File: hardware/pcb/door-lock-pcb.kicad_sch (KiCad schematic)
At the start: 53 parts, among them J1 105162-0001, J2 Conn_01x08, J4 Conn_01x04, J6 Conn_01x02, J7 Conn_01x02, Q1 SI2308DS, Q3 DMN6068LK3, U1 ESP32-DEVKIT-V1, U2 DS1307Z+, U3 MP1470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

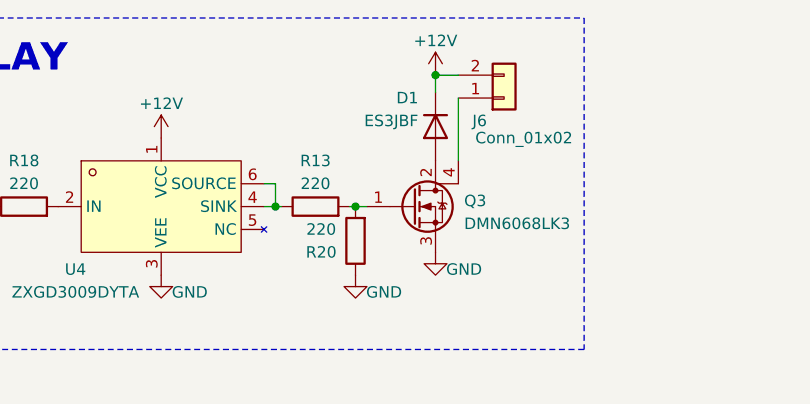
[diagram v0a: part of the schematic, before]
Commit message: fixed error with mosfet drain
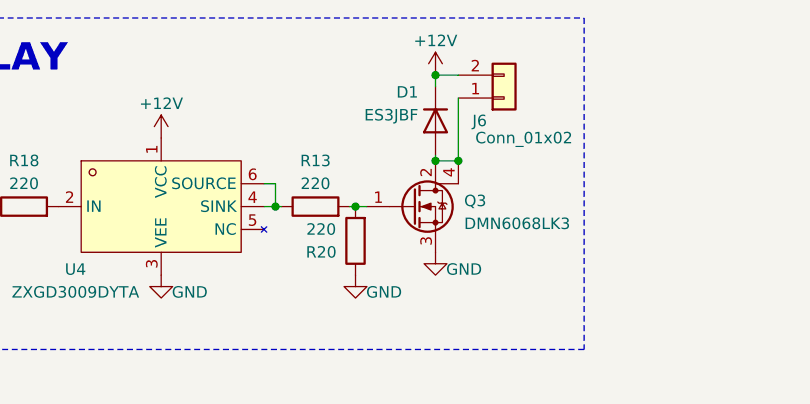
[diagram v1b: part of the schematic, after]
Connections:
- net at J6.1 (Pin_1), Q3.4 (D): now also D1.2 (A), Q3.2 (D)
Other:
- moved on the sheet: D1
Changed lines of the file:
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@@
   (junction (at 50.165 124.46) (diameter 0) (color 0 0 0 0)
   )
+  (junction (at 179.705 32.385) (diameter 0) (color 0 0 0 0)
+  )
   (junction (at 52.07 189.23) (diameter 0) (color 0 0 0 0)
   )
   (junction (at 186.055 134.62) (diameter 0) (color 0 0 0 0)
+  )
+  (junction (at 177.165 32.385) (diameter 0) (color 0 0 0 0)
   )
   (junction (at 215.265 137.16) (diameter 0) (color 0 0 0 0)
@@
     (stroke (width 0) (type default))
   )
+  (wire (pts (xy 177.165 31.75) (xy 177.165 32.385))
+    (stroke (width 0) (type default))
+  )
   (wire (pts (xy 186.055 144.78) (xy 186.055 139.7))
     (stroke (width 0) (type default))
@@
     (stroke (width 0) (type default))
   )
+  (wire (pts (xy 177.165 32.385) (xy 179.705 32.385))
+    (stroke (width 0) (type default))
+  )
   (wire (pts (xy 168.275 37.465) (xy 169.545 37.465))
     (stroke (width 0) (type default))
@@
     (stroke (width 0) (type default))
   )
-  (wire (pts (xy 177.165 22.86) (xy 177.165 24.765))
+  (wire (pts (xy 177.165 22.86) (xy 177.165 24.13))
     (stroke (width 0) (type default))
   )
@@
     )
   )
-  (symbol (lib_id "Device:D") (at 177.165 28.575 90) (mirror x) (unit 1)
-    (in_bom yes) (on_board yes) (dnp no)
-    (property "Reference" "D1" (at 175.26 25.4 90)
-      (effects (font (size 1.27 1.27)) (justify left))
-    )
-    (property "Value" "ES3JBF" (at 175.26 27.94 90)
-      (effects (font (size 1.27 1.27)) (justify left))
-    )
-    (property "Footprint" "Diode_SMD:D_SMC" (at 177.165 28.575 0)
-      (effects (font (size 1.27 1.27)) hide)
-    )
-    (property "Datasheet" "~" (at 177.165 28.575 0)
-      (effects (font (size 1.27 1.27)) hide)
-    )
-    (property "Sim.Device" "D" (at 177.165 28.575 0)
-      (effects (font (size 1.27 1.27)) hide)
-    )
-    (property "Sim.Pins" "1=K 2=A" (at 177.165 28.575 0)
-      (effects (font (size 1.27 1.27)) hide)
-    )
-    (property "LCSC" "C3011135" (at 177.165 28.575 90)
-      (effects (font (size 1.27 1.27)) hide)
-    )
+  (symbol (lib_id "Device:D") (at 177.165 27.94 90) (mirror x) (unit 1)
+    (in_bom yes) (on_board yes) (dnp no)
+    (property "Reference" "D1" (at 175.26 24.765 90)
+      (effects (font (size 1.27 1.27)) (justify left))
+    )
+    (property "Value" "ES3JBF" (at 175.26 27.305 90)
+      (effects (font (size 1.27 1.27)) (justify left))
+    )
+    (property "Footprint" "Diode_SMD:D_SMC" (at 177.165 27.94 0)
+      (effects (font (size 1.27 1.27)) hide)
+    )
+    (property "Datasheet" "~" (at 177.165 27.94 0)
+      (effects (font (size 1.27 1.27)) hide)
+    )
+    (property "Sim.Device" "D" (at 177.165 27.94 0)
+      (effects (font (size 1.27 1.27)) hide)
+    )
+    (property "Sim.Pins" "1=K 2=A" (at 177.165 27.94 0)
+      (effects (font (size 1.27 1.27)) hide)
+    )
+    (property "LCSC" "C3011135" (at 177.165 27.94 90)
+      (effects (font (size 1.27 1.27)) hide)
+    )
